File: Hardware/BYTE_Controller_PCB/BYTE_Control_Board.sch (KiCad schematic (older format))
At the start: 31 parts, among them J1 8P8C_Shielded, J2 Battery, J3 Expansion, J4 SWD, P1 USB_C_Plug_USB2.0, Q1 DMC2400UV, SW1 GPIO, SW2 GPIO, SW3 RST, U1 MCP73830T-2AAI_MYY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

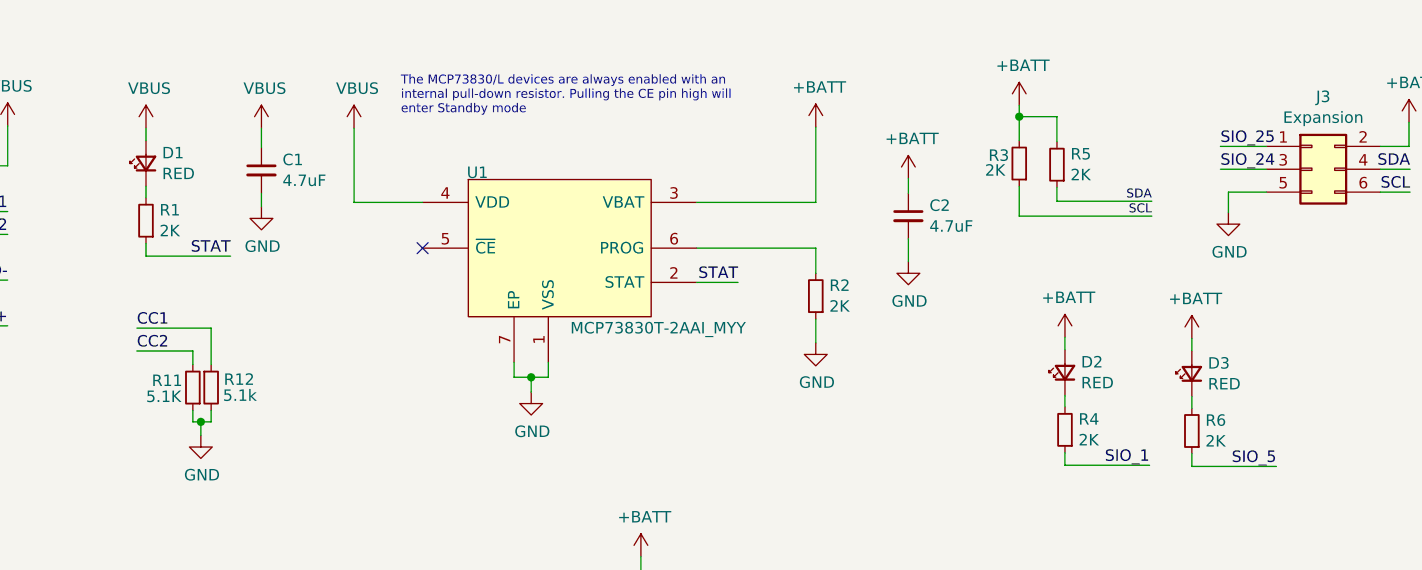
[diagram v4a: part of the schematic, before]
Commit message: add manufacturer part number for BOM
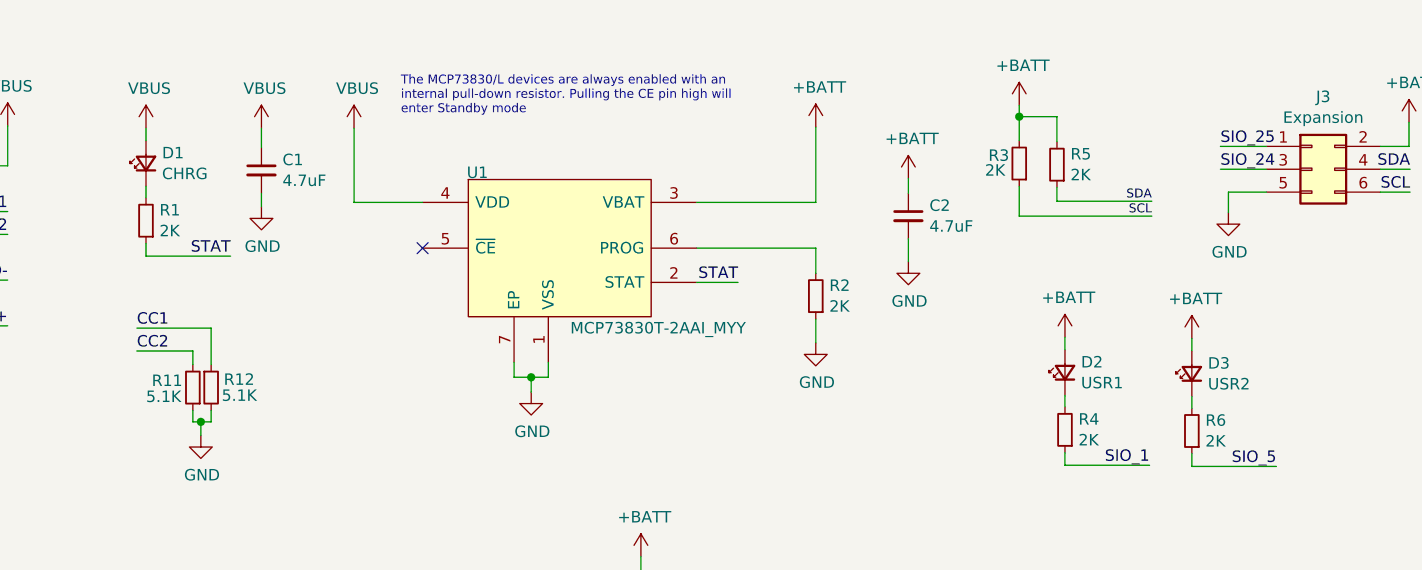
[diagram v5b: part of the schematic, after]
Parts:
- C1, C2, C3: manf# (none) -> CM105X6T475M16AT
- C4: manf# (none) -> CL10B104KA8NNNC
- D1: value RED -> CHRG; manf# (none) -> LS R976-NR-1
- D2: value RED -> USR1; manf# (none) -> LTST-S220KGKT
- D3: value RED -> USR2; manf# (none) -> LTST-C170TBKT
- J2, J3, J4: manf# (none) -> -
- P1: manf# (none) -> C393939
- Q1: manf# (none) -> DMC2400UV-7
- R1, R10, R2, R3, R4, R5, R6, R7, R8, R9: manf# (none) -> RMCF0603FT2K05
- R11: manf# (none) -> RMCF0603FT5K10
- R12: value 5.1k -> 5.1K; manf# (none) -> RMCF0603FT5K10
- R13: manf# (none) -> RMCF0603FT10K0
- SW1, SW2: manf# (none) -> TL3305AF260QG
- SW3: manf# (none) -> KMR211NGLFS
- U2: manf# (none) -> 453-00041R
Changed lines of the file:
@@
 F 2 "Controller:BL653_v5" H 9610 1455 50  0001 C CNN
 F 3 "https://www.lairdconnect.com/documentation/datasheet-bl653-series" H 9560 1355 50  0001 C CNN
+F 4 "453-00041R" H 9610 2655 50  0001 C CNN "manf#"
 	1    9610 2655
 	1    0    0    -1
@@
 F 2 "Resistor_SMD:R_0603_1608Metric" H 5380 1580 50  0001 C CNN
 F 3 "~" H 5380 1580 50  0001 C CNN
+F 4 "RMCF0603FT2K05" H 5380 1580 50  0001 C CNN "manf#"
 	1    5380 1580
 	-1   0    0    1
@@
 F 2 "Capacitor_SMD:C_0603_1608Metric" H 5785 1230 50  0001 C CNN
 F 3 "~" H 5785 1230 50  0001 C CNN
+F 4 "CM105X6T475M16AT" H 5785 1230 50  0001 C CNN "manf#"
 	1    5785 1230
 	1    0    0    -1
@@
 F 2 "Capacitor_SMD:C_0603_1608Metric" H 2955 1030 50  0001 C CNN
 F 3 "~" H 2955 1030 50  0001 C CNN
+F 4 "CM105X6T475M16AT" H 2955 1030 50  0001 C CNN "manf#"
 	1    2955 1030
 	1    0    0    -1
@@
 P 2450 1000
 F 0 "D1" V 2496 930 50  0000 R CNN
-F 1 "RED" V 2405 930 50  0000 R CNN
+F 1 "CHRG" V 2405 930 50  0000 R CNN
 F 2 "LED_SMD:LED_0805_2012Metric" V 2450 1000 50  0001 C CNN
 F 3 "~" V 2450 1000 50  0001 C CNN
+F 4 "LS R976-NR-1" H 2450 1000 50  0001 C CNN "manf#"
 	1    2450 1000
 	0    -1   -1   0
@@
 F 2 "Resistor_SMD:R_0603_1608Metric" H 2450 1250 50  0001 C CNN
 F 3 "~" H 2450 1250 50  0001 C CNN
+F 4 "RMCF0603FT2K05" H 2450 1250 50  0001 C CNN "manf#"
 	1    2450 1250
 	-1   0    0    1
@@
 F 2 "Resistor_SMD:R_0603_1608Metric" H 6270 1000 50  0001 C CNN
 F 3 "~" H 6270 1000 50  0001 C CNN
+F 4 "RMCF0603FT2K05" H 6270 1000 50  0001 C CNN "manf#"
 	1    6270 1000
 	-1   0    0    1
@@
 F 2 "Resistor_SMD:R_0603_1608Metric" H 6435 1005 50  0001 C CNN
 F 3 "~" H 6435 1005 50  0001 C CNN
+F 4 "RMCF0603FT2K05" H 6435 1005 50  0001 C CNN "manf#"
 	1    6435 1005
 	-1   0    0    1
@@
 P 6470 1915
 F 0 "D2" V 6516 1845 50  0000 R CNN
-F 1 "RED" V 6425 1845 50  0000 R CNN
+F 1 "USR1" V 6425 1845 50  0000 R CNN
 F 2 "LED_SMD:LED_0805_2012Metric" V 6470 1915 50  0001 C CNN
 F 3 "~" V 6470 1915 50  0001 C CNN
+F 4 "LTST-S220KGKT" H 6470 1915 50  0001 C CNN "manf#"
 	1    6470 1915
 	0    -1   -1   0
@@
 F 2 "Resistor_SMD:R_0603_1608Metric" H 6470 2165 50  0001 C CNN
 F 3 "~" H 6470 2165 50  0001 C CNN
+F 4 "RMCF0603FT2K05" H 6470 2165 50  0001 C CNN "manf#"
 	1    6470 2165
 	-1   0    0    1
@@
 F 2 "Button_Switch_SMD:SW_SPST_TL3305A" H 7040 3445 50  0001 C CNN
 F 3 "~" H 7040 3445 50  0001 C CNN
+F 4 "TL3305AF260QG" H 7040 3245 50  0001 C CNN "manf#"
 	1    7040 3245
 	0    1    1    0
@@
 F 2 "Button_Switch_SMD:SW_SPST_TL3305A" H 6515 3450 50  0001 C CNN
 F 3 "~" H 6515 3450 50  0001 C CNN
+F 4 "TL3305AF260QG" H 6515 3250 50  0001 C CNN "manf#"
 	1    6515 3250
 	0    1    1    0
@@
 P 7025 1920
 F 0 "D3" V 7071 1850 50  0000 R CNN
-F 1 "RED" V 6980 1850 50  0000 R CNN
+F 1 "USR2" V 6980 1850 50  0000 R CNN
 F 2 "LED_SMD:LED_0805_2012Metric" V 7025 1920 50  0001 C CNN
 F 3 "~" V 7025 1920 50  0001 C CNN
+F 4 "LTST-C170TBKT" H 7025 1920 50  0001 C CNN "manf#"
 	1    7025 1920
 	0    -1   -1   0
@@
 F 2 "Resistor_SMD:R_0603_1608Metric" H 7025 2170 50  0001 C CNN
 F 3 "~" H 7025 2170 50  0001 C CNN
+F 4 "RMCF0603FT2K05" H 7025 2170 50  0001 C CNN "manf#"
 	1    7025 2170
 	-1   0    0    1
@@
 F 2 "Connector_PinHeader_2.54mm:PinHeader_1x02_P2.54mm_Vertical" H 945 3540 50  0001 C CNN
 F 3 "~" H 945 3540 50  0001 C CNN
+F 4 "-" H 945 3540 50  0001 C CNN "manf#"
 	1    945  3540
 	-1   0    0    1
@@
 F 2 "Resistor_SMD:R_0603_1608Metric" H 3805 3715 50  0001 C CNN
 F 3 "~" H 3805 3715 50  0001 C CNN
+F 4 "RMCF0603FT2K05" H 3805 3715 50  0001 C CNN "manf#"
 	1    3805 3715
 	-1   0    0    1
@@
 F 2 "Package_TO_SOT_SMD:SOT-563" H 4715 3150 50  0001 L CNN
 F 3 "" H 4615 3225 50  0001 L CNN
+F 4 "DMC2400UV-7" H 4515 3225 50  0001 C CNN "manf#"
 	2    4515 3225
 	1    0    0    -1
@@
 F 2 "Package_TO_SOT_SMD:SOT-563" H 4285 3440 50  0001 L CNN
 F 3 "" H 4185 3515 50  0001 L CNN
+F 4 "DMC2400UV-7" H 4085 3515 50  0001 C CNN "manf#"
 	1    4085 3515
 	1    0    0    -1
@@
 F 2 "Resistor_SMD:R_0603_1608Metric" H 4185 3020 50  0001 C CNN
 F 3 "~" H 4185 3020 50  0001 C CNN
+F 4 "RMCF0603FT2K05" H 4185 3020 50  0001 C CNN "manf#"
 	1    4185 3020
 	-1   0    0    1
@@
 F 2 "Resistor_SMD:R_0603_1608Metric" H 4615 3600 50  0001 C CNN
 F 3 "~" H 4615 3600 50  0001 C CNN
+F 4 "RMCF0603FT2K05" H 4615 3600 50  0001 C CNN "manf#"
 	1    4615 3600
 	-1   0    0    1
@@
 F 2 "Resistor_SMD:R_0603_1608Metric" H 4615 3930 50  0001 C CNN
 F 3 "~" H 4615 3930 50  0001 C CNN
+F 4 "RMCF0603FT2K05" H 4615 3930 50  0001 C CNN "manf#"
 	1    4615 3930
 	-1   0    0    1
@@
 F 2 "Connectors:C393939" H 1215 1610 50  0001 C CNN
 F 3 "https://www.usb.org/sites/default/files/documents/usb_type-c.zip" H 1215 1610 50  0001 C CNN
+F 4 "C393939" H 1065 1610 50  0001 C CNN "manf#"
 	1    1065 1610
 	1    0    0    -1
@@
 F 2 "Resistor_SMD:R_0603_1608Metric" H 2655 1980 50  0001 C CNN
 F 3 "~" H 2655 1980 50  0001 C CNN
+F 4 "RMCF0603FT5K10" H 2655 1980 50  0001 C CNN "manf#"
 	1    2655 1980
 	-1   0    0    1
@@
 P 2735 1980
 F 0 "R12" H 2925 2015 50  0000 R CNN
-F 1 "5.1k" H 2935 1945 50  0000 R CNN
+F 1 "5.1K" H 2935 1945 50  0000 R CNN
 F 2 "Resistor_SMD:R_0603_1608Metric" H 2735 1980 50  0001 C CNN
 F 3 "~" H 2735 1980 50  0001 C CNN
+F 4 "RMCF0603FT5K10" H 2735 1980 50  0001 C CNN "manf#"
 	1    2735 1980
 	1    0    0    -1
@@
 F 2 "Capacitor_SMD:C_0603_1608Metric" H 8375 900 50  0001 C CNN
 F 3 "~" H 8375 900 50  0001 C CNN
+F 4 "CM105X6T475M16AT" H 8375 900 50  0001 C CNN "manf#"
 	1    8375 900
 	1    0    0    -1
@@
 F 2 "Capacitor_SMD:C_0603_1608Metric" H 10880 1000 50  0001 C CNN
 F 3 "~" H 10880 1000 50  0001 C CNN
+F 4 "CL10B104KA8NNNC" H 10880 1000 50  0001 C CNN "manf#"
 	1    10880 1000
 	1    0    0    -1
@@
 F 2 "Button_Switch_SMD:SW_Push_1P1T-SH_NO_CK_KMR2xxG" H 7030 4860 50  0001 C CNN
 F 3 "~" H 7030 4860 50  0001 C CNN
+F 4 "KMR211NGLFS" H 7030 4660 50  0001 C CNN "manf#"
 	1    7030 4660
 	0    1    1    0
@@
 F 2 "Resistor_SMD:R_0603_1608Metric" H 7030 4150 50  0001 C CNN
 F 3 "~" H 7030 4150 50  0001 C CNN
+F 4 "RMCF0603FT10K0" H 7030 4150 50  0001 C CNN "manf#"
 	1    7030 4150
 	-1   0    0    1
@@
 F 2 "Connector_PinHeader_2.54mm:PinHeader_2x03_P2.54mm_Vertical" H 7550 1025 50  0001 C CNN
 F 3 "~" H 7550 1025 50  0001 C CNN
+F 4 "-" H 7550 1025 50  0001 C CNN "manf#"
 	1    7550 1025
 	1    0    0    -1
@@
 F 2 "Connector_PinHeader_2.54mm:PinHeader_1x04_P2.54mm_Vertical" H 4680 5015 50  0001 C CNN
 F 3 "~" H 4680 5015 50  0001 C CNN
+F 4 "-" H 4680 5015 50  0001 C CNN "manf#"
 	1    4680 5015
 	1    0    0    -1
